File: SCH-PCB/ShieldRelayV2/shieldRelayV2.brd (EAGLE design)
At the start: 99.1 x 84.1 mm, 90 parts, among them IC1 LM2596SX-5.0_NOPB, IC2 LM1117MPX-33NOPB, IC3 FT231XS-R, K1 SLA-05VDC-SL-C, K2 SRD-05VDC-SL-C, K3 G3MB-202PL-DC5, K5 G3MB-202PL-DC5, K6 SRD-05VDC-SL-C, Q1 MMST2222A-7-F, Q2 MMST2222A-7-F, Q3 MMST2222A-7-F, Q4 MMST2222A-7-F, Q5 MMST2222A-7-F, Q6 MMBT3904-TP, Q7 MMBT3904-TP

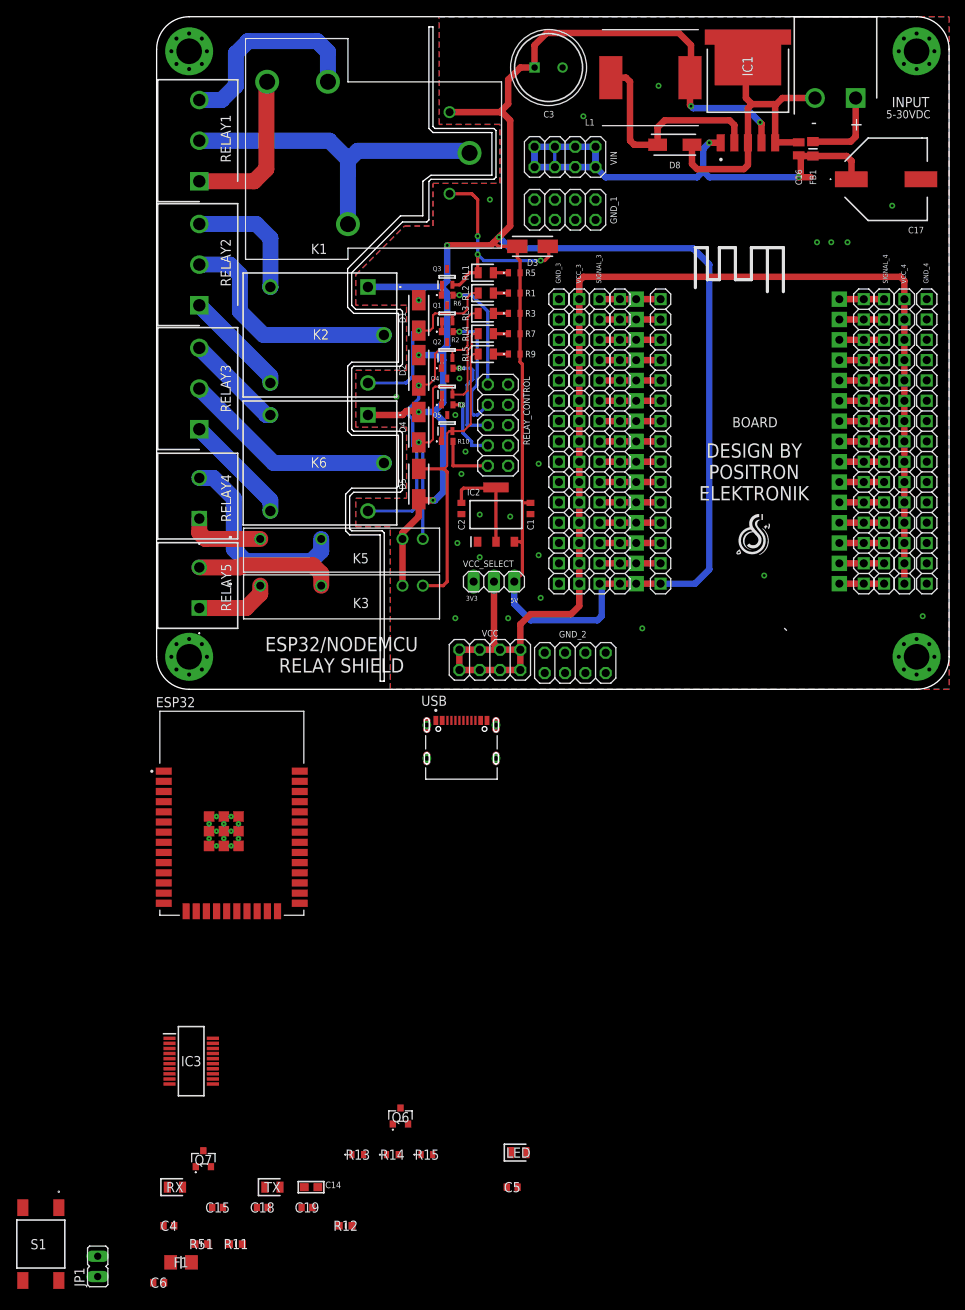
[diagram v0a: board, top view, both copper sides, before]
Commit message: FEAT: update sch, board, gerber adn bom for esp embedded to pcb
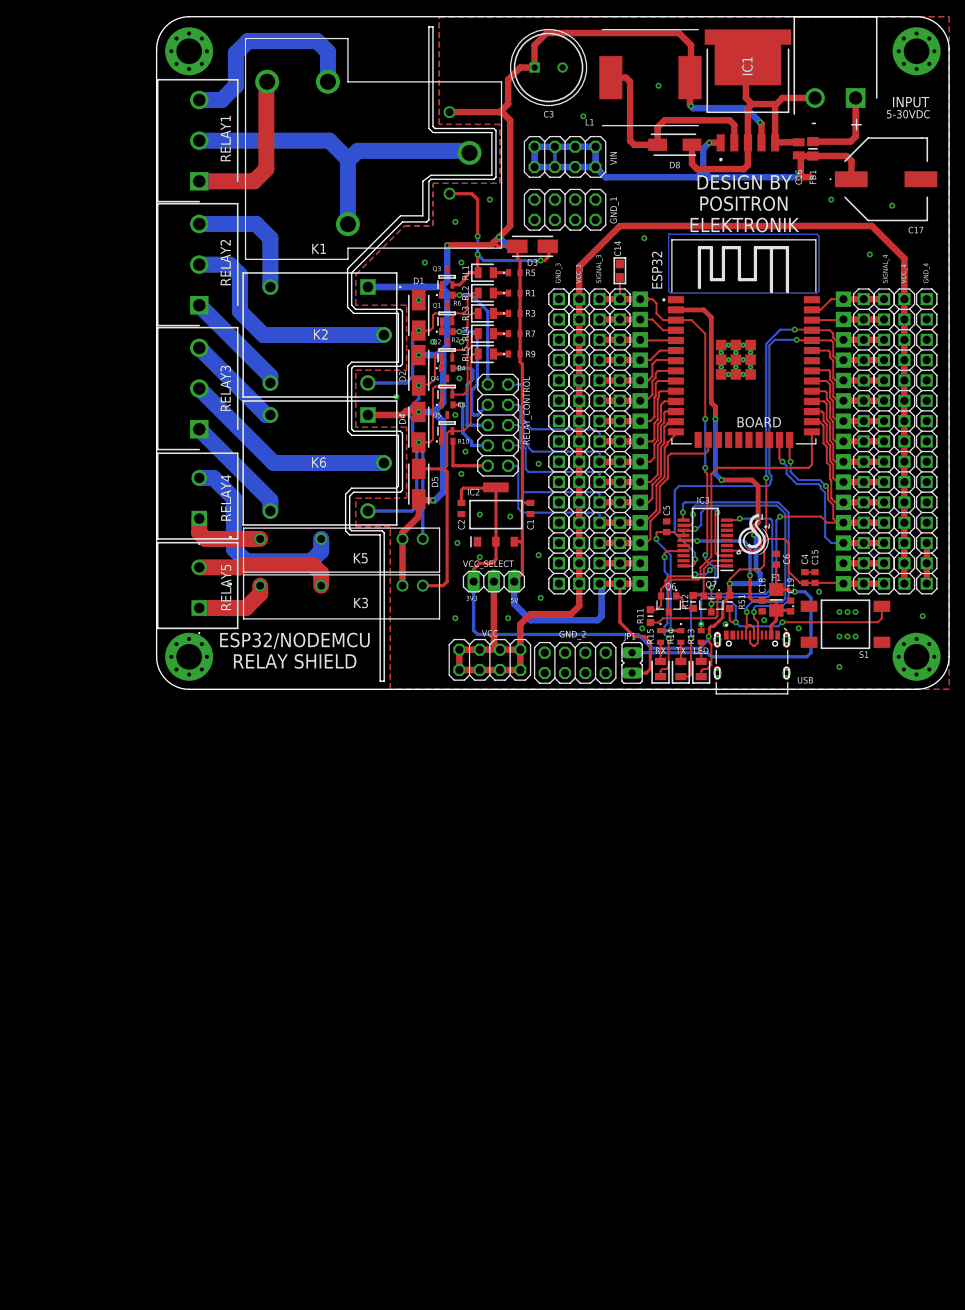
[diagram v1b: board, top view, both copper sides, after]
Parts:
- removed JP13: (no value), pinhead_mod:1X15
- moved S1 127.0 mm to (86.1, 24.1), turned to 90 degrees
- moved C14 120.9 mm to (57.9, 68.3), turned to 90 degrees
- moved C6 118.9 mm to (77.5, 32.3), turned to 90 degrees
- moved C4 113.5 mm to (81.0, 30.0), turned to 270 degrees
- moved F1 111.3 mm to (77.5, 27.2), turned to 90 degrees
- moved C15 108.5 mm to (82.3, 30.0), turned to 270 degrees
- moved R51 103.9 mm to (71.6, 26.9), turned to 270 degrees
- moved JP1 100.8 mm to (59.4, 19.3), turned to 180 degrees
- moved C18 97.8 mm to (75.7, 26.4), turned to 90 degrees
- moved C19 96.5 mm to (79.2, 26.4), turned to 90 degrees
- moved R11 94.0 mm to (61.7, 25.1), turned to 270 degrees
- moved Q7 94.0 mm to (69.3, 26.7), turned to 180 degrees
- moved IC3 91.2 mm to (68.6, 34.3), turned to 180 degrees
- moved R12 89.3 mm to (67.1, 26.9), turned to 270 degrees
- moved RX 88.8 mm to (63.0, 18.5), turned to 90 degrees
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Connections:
- removed net 1: BOARD.3V3, JP11.1, SIGNAL_4.1
- removed net 2: BOARD.GND@1, JP11.2, SIGNAL_4.2
- removed net 3.3V: C15.2, C4.2, ESP32.2, LED.1, R51.1
- removed net 3V3_FTDI: IC3.3
- removed net BUTTON1: ESP32.30
- removed net D23: ESP32.37
- removed net D25: ESP32.10
- removed net D26: ESP32.11
- removed net D27: ESP32.12
- removed net D32: ESP32.8
- removed net D33: ESP32.9
- removed net D34: ESP32.6
- removed net D35: ESP32.7
- removed net D5: ESP32.29
- removed net EN: C14.1, ESP32.3, Q7.3, R51.2, S1.2
- removed net LED: ESP32.31, R13.1
- removed net N$23: RELAY_CONTROL.10
- removed net N$24: RELAY_CONTROL.8
- removed net N$25: RELAY_CONTROL.6
- removed net N$26: RELAY_CONTROL.4
- removed net N$27: RELAY_CONTROL.2
- removed net RX_DWM: ESP32.28
- removed net SCL: ESP32.36
- removed net SDA: ESP32.33
- removed net SD_HOST_CLK: ESP32.13
- removed net SD_HOST_CMD: ESP32.23
- removed net SD_HOST_D0: ESP32.24
- removed net SD_HOST_D1: ESP32.26
- removed net SD_HOST_D2: ESP32.14
- removed net SD_HOST_D3: ESP32.16
- removed net TX_DWM: ESP32.27
- removed net U0RXD: ESP32.34, IC3.20
- removed net U0TXD: ESP32.35, IC3.4
- removed net VN: ESP32.5
- removed net VP: ESP32.4
- net +3V3: now also BOARD.3V3, C15.2, C4.2, ESP32.2, JP11.1, LED.1, R51.1, SIGNAL_4.1
- net +5V: no longer JP13.1
- net 10: now also ESP32.31
- net 11: now also ESP32.33
- net 12: now also ESP32.34, IC3.20
- net 13: now also ESP32.35, IC3.4
- net 14: now also ESP32.36
- net 15: now also ESP32.37
- net 18: now also ESP32.16; no longer JP13.3
- net 19: now also ESP32.14, RELAY_CONTROL.10; no longer JP13.4
- net 20: now also ESP32.13, RELAY_CONTROL.8; no longer JP13.5
- net 21: now also ESP32.12, RELAY_CONTROL.6; no longer JP13.6
- net 22: now also ESP32.11, RELAY_CONTROL.4; no longer JP13.7
- net 23: now also ESP32.10, RELAY_CONTROL.2; no longer JP13.8
- net 24: now also ESP32.9; no longer JP13.9
- net 25: now also ESP32.8; no longer JP13.10
- net 26: now also ESP32.7; no longer JP13.11
- net 27: now also ESP32.6; no longer JP13.12
- net 28: now also ESP32.5; no longer JP13.13
- net 29: now also ESP32.4; no longer JP13.14
- net 3: now also ESP32.23
- net 30: now also C14.1, ESP32.3, Q7.3, R51.2, S1.2; no longer JP13.15
- net 3V3_OUT: now also IC3.3
- net 4: now also ESP32.24, R13.1
- net 5: now also ESP32.26
- net 6: now also ESP32.27
- net 7: now also ESP32.28
- net 8: now also ESP32.29
- net 9: now also ESP32.30
- net GND: now also BOARD.GND@1, JP11.2, SIGNAL_4.2; no longer JP13.2
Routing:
- net +3V3: track 12.8 -> 145.8 mm, vias 0 -> 5
- net 30: track 7.62 -> 82.4 mm, vias 0 -> 7
- net +5V: track 302.4 -> 244.7 mm
- net 12: track 5.59 -> 58.2 mm, vias 0 -> 2
- net N$21: track 0.00 -> 51.9 mm
- net 4: track 5.59 -> 50.8 mm, vias 0 -> 4
- net 13: track 5.59 -> 46.4 mm, vias 0 -> 2
- net 0: track 0.00 -> 38.7 mm
- net D+: track 0.00 -> 38.3 mm, vias 0 -> 2
- net VBUS_: track 0.00 -> 37.5 mm, vias 0 -> 1
- net D-: track 0.00 -> 36.7 mm, vias 0 -> 2
- net CBUS2: track 0.00 -> 35.9 mm, vias 0 -> 2
- net 3V3_OUT: track 0.00 -> 33.0 mm, vias 0 -> 4
- net 19: track 7.62 -> 36.5 mm
- net 20: track 7.62 -> 36.1 mm
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
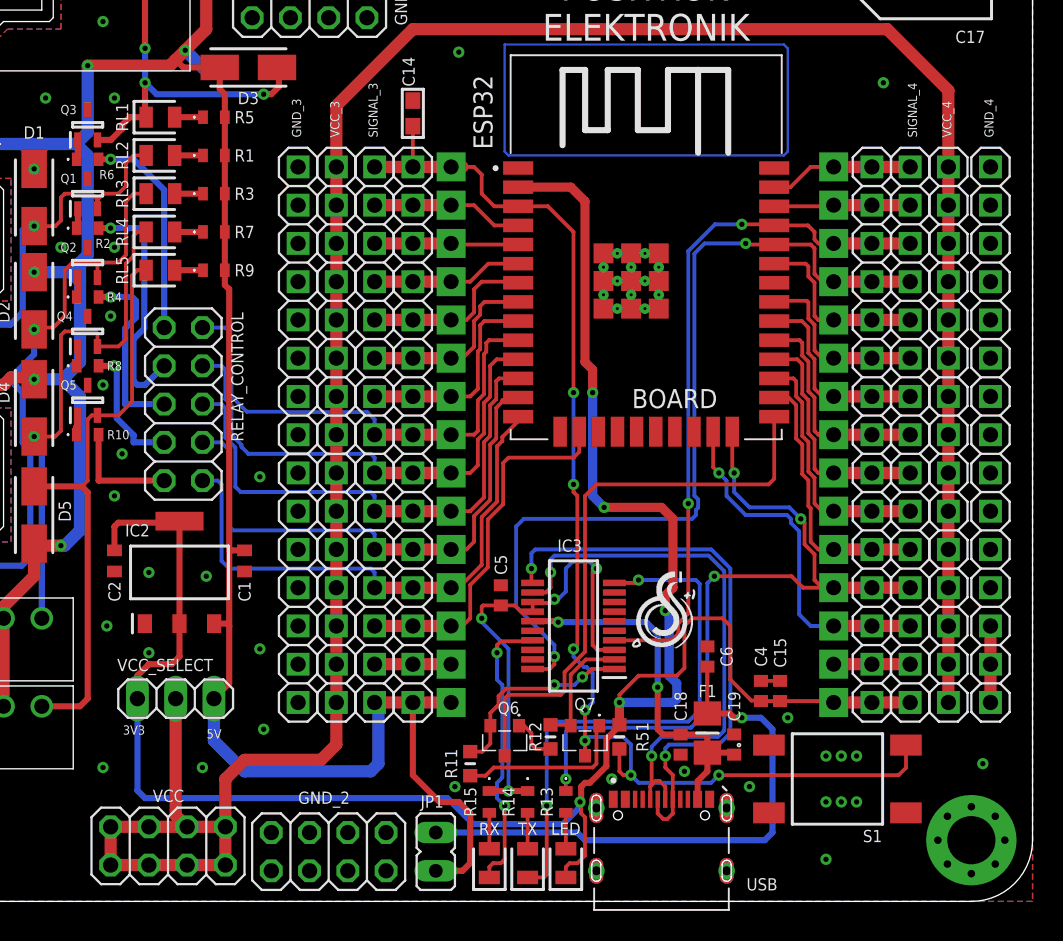
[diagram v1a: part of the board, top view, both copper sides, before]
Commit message: FIX: fix minor pcb
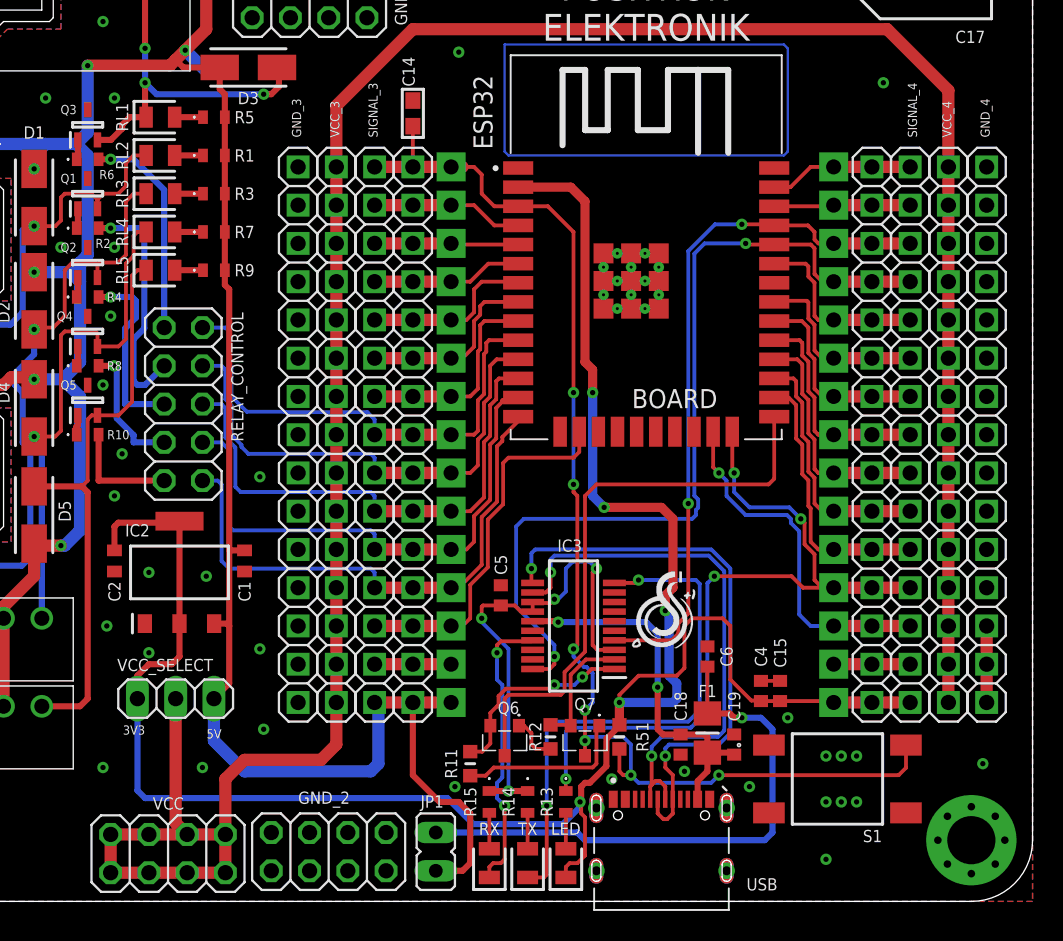
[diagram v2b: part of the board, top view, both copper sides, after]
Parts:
- moved VCC 0.51 mm to (41.7, 19.2)
- moved GND_4 0.25 mm to (96.0, 47.0)
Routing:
- net N$39: track 168.1 -> 169.1 mm
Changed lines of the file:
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@@
 <drawing>
 <settings>
-<setting alwaysvectorfont="yes"/>
+<setting alwaysvectorfont="no"/>
 <setting verticaltext="up"/>
 </settings>
@@
 <attribute name="VALUE" x="96.647" y="27.94" size="1.27" layer="27" rot="R90"/>
 </element>
-<element name="GND_4" library="pinhead_mod" package="1X15" package3d_urn="urn:adsk.eagle:package:22424/2" value="" x="96.266" y="46.99" smashed="yes" rot="R270">
-<attribute name="NAME" x="96.4692" y="66.7258" size="0.6096" layer="25" ratio="10" rot="R90"/>
-<attribute name="POPULARITY" value="4" x="96.266" y="46.99" size="1.778" layer="27" rot="R270" display="off"/>
-<attribute name="VALUE" x="93.091" y="66.04" size="1.27" layer="27" rot="R270"/>
+<element name="GND_4" library="pinhead_mod" package="1X15" package3d_urn="urn:adsk.eagle:package:22424/2" value="" x="96.012" y="46.99" smashed="yes" rot="R270">
+<attribute name="NAME" x="96.2152" y="66.7258" size="0.6096" layer="25" ratio="10" rot="R90"/>
+<attribute name="POPULARITY" value="4" x="96.012" y="46.99" size="1.778" layer="27" rot="R270" display="off"/>
+<attribute name="VALUE" x="92.837" y="66.04" size="1.27" layer="27" rot="R270"/>
 </element>
 <element name="GND_3" library="pinhead_mod" package="1X15" package3d_urn="urn:adsk.eagle:package:22424/2" value="" x="50.292" y="46.99" smashed="yes" rot="R270">
@@
 <attribute name="VALUE" x="45.974" y="32.639" size="1.27" layer="27" rot="R180"/>
 </element>
-<element name="VCC" library="pinhead" library_urn="urn:adsk.eagle:library:325" package="2X04" package3d_urn="urn:adsk.eagle:package:22461/2" value="" x="41.656" y="19.685" smashed="yes">
-<attribute name="NAME" x="40.64" y="22.606" size="0.8128" layer="25" ratio="10"/>
-<attribute name="POPULARITY" value="47" x="41.656" y="19.685" size="1.778" layer="27" display="off"/>
-<attribute name="VALUE" x="36.576" y="15.24" size="1.27" layer="27"/>
+<element name="VCC" library="pinhead" library_urn="urn:adsk.eagle:library:325" package="2X04" package3d_urn="urn:adsk.eagle:package:22461/2" value="" x="41.656" y="19.177" smashed="yes">
+<attribute name="NAME" x="40.64" y="22.098" size="0.8128" layer="25" ratio="10"/>
+<attribute name="POPULARITY" value="47" x="41.656" y="19.177" size="1.778" layer="27" display="off"/>
+<attribute name="VALUE" x="36.576" y="14.732" size="1.27" layer="27"/>
 </element>
 <element name="GND_2" library="pinhead" library_urn="urn:adsk.eagle:library:325" package="2X04" package3d_urn="urn:adsk.eagle:package:22461/2" value="" x="52.324" y="19.304" smashed="yes">
@@
 <wire x1="85.852" y1="31.75" x2="88.392" y2="31.75" width="0.8128" layer="1"/>
 <wire x1="90.932" y1="31.75" x2="88.392" y2="31.75" width="0.8128" layer="1"/>
-<wire x1="96.266" y1="31.75" x2="96.266" y2="34.29" width="0.8128" layer="1"/>
-<wire x1="96.266" y1="29.21" x2="96.266" y2="31.75" width="0.8128" layer="1"/>
+<wire x1="96.012" y1="31.75" x2="96.012" y2="34.29" width="0.8128" layer="1"/>
+<wire x1="96.012" y1="29.21" x2="96.012" y2="31.75" width="0.8128" layer="1"/>
 <via x="85.344" y="22.606" extent="1-16" drill="0.35"/>
 <via x="85.344" y="25.654" extent="1-16" drill="0.35"/>
@@
 <contactref element="VCC" pad="3"/>
 <contactref element="VCC" pad="1"/>
-<wire x1="42.164" y1="29.464" x2="42.164" y2="21.717" width="0.8128" layer="1"/>
-<wire x1="42.164" y1="21.717" x2="42.926" y2="20.955" width="0.8128" layer="1"/>
-<wire x1="40.386" y1="20.955" x2="42.926" y2="20.955" width="0.8128" layer="1"/>
-<wire x1="40.386" y1="20.955" x2="37.846" y2="20.955" width="0.8128" layer="1"/>
-<wire x1="37.846" y1="20.955" x2="37.846" y2="18.415" width="0.8128" layer="1"/>
-<wire x1="37.846" y1="18.415" x2="40.386" y2="18.415" width="0.8128" layer="1"/>
-<wire x1="40.386" y1="18.415" x2="42.926" y2="18.415" width="0.8128" layer="1"/>
-<wire x1="42.926" y1="18.415" x2="45.466" y2="18.415" width="0.8128" layer="1"/>
-<wire x1="45.466" y1="18.415" x2="45.466" y2="20.955" width="0.8128" layer="1"/>
-<wire x1="45.466" y1="20.955" x2="42.926" y2="20.955" width="0.8128" layer="1"/>
+<wire x1="42.164" y1="29.464" x2="42.164" y2="21.209" width="0.8128" layer="1"/>
+<wire x1="42.164" y1="21.209" x2="42.926" y2="20.447" width="0.8128" layer="1"/>
+<wire x1="40.386" y1="20.447" x2="42.926" y2="20.447" width="0.8128" layer="1"/>
+<wire x1="40.386" y1="20.447" x2="37.846" y2="20.447" width="0.8128" layer="1"/>
+<wire x1="37.846" y1="20.447" x2="37.846" y2="17.907" width="0.8128" layer="1"/>
+<wire x1="37.846" y1="17.907" x2="40.386" y2="17.907" width="0.8128" layer="1"/>
+<wire x1="40.386" y1="17.907" x2="42.926" y2="17.907" width="0.8128" layer="1"/>
+<wire x1="42.926" y1="17.907" x2="45.466" y2="17.907" width="0.8128" layer="1"/>
+<wire x1="45.466" y1="17.907" x2="45.466" y2="20.447" width="0.8128" layer="1"/>
+<wire x1="45.466" y1="20.447" x2="42.926" y2="20.447" width="0.8128" layer="1"/>
 <wire x1="51.816" y1="25.4" x2="52.832" y2="26.416" width="0.8128" layer="1"/>
 <wire x1="52.832" y1="26.416" x2="52.832" y2="29.21" width="0.8128" layer="1"/>
@@
 <wire x1="93.472" y1="34.29" x2="93.472" y2="31.75" width="0.8128" layer="1"/>
 <wire x1="93.472" y1="29.21" x2="93.472" y2="31.75" width="0.8128" layer="1"/>
-<wire x1="45.466" y1="20.955" x2="45.466" y2="24.13" width="0.8128" layer="1"/>
+<wire x1="45.466" y1="20.447" x2="45.466" y2="24.13" width="0.8128" layer="1"/>
 <wire x1="45.466" y1="24.13" x2="46.736" y2="25.4" width="0.8128" layer="1"/>
 <wire x1="46.736" y1="25.4" x2="51.816" y2="25.4" width="0.8128" layer="1"/>

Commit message: FIX: fix gnd pin on ic 1117 that no connected
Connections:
- net GND: now also IC2.1
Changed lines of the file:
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@@
 </layers>
 <board>
-<fusionsync huburn="a.YnVzaW5lc3M6Z21haWwyMzM3NTk" projecturn="a.YnVzaW5lc3M6Z21haWwyMzM3NTkjRDIwMTkwNzEwMjAyOTg4NzI2" f3durn="urn:adsk.wipprod:dm.lineage:9T0BP-n2RnCNxMkO3_9ujQ" pcbguid="" lastpulledtime="" lastsyncedchangeguid="" latestrevisionid="43e5cbbb-d091-4418-b876-1ea316f0a193" lastsyncedrevisionid="43e5cbbb-d091-4418-b876-1ea316f0a193" lastboardhashguid="19c69a16-bb44-e2b6-368f-cff3622da438" lastpushedtime="2024-06-15T15:23:29Z" linktopcb3d="true"/>
+<fusionsync huburn="a.YnVzaW5lc3M6Z21haWwyMzM3NTk" projecturn="a.YnVzaW5lc3M6Z21haWwyMzM3NTkjRDIwMTkwNzEwMjAyOTg4NzI2" f3durn="urn:adsk.wipprod:dm.lineage:9T0BP-n2RnCNxMkO3_9ujQ" pcbguid="" lastpulledtime="" lastsyncedchangeguid="" latestrevisionid="43e5cbbb-d091-4418-b876-1ea316f0a193" lastsyncedrevisionid="43e5cbbb-d091-4418-b876-1ea316f0a193" lastboardhashguid="19c69a16-bb44-e2b6-368f-cff3622da438" lastpushedtime="2024-06-15T15:23:29Z" linktopcb3d="false"/>
 <plain>
 <wire x1="78.74" y1="23.368" x2="78.486" y2="23.622" width="0.1524" layer="21"/>
@@
 <via x="38.1" y="59.436" extent="1-16" drill="0.35"/>
 <via x="34.544" y="59.436" extent="1-16" drill="0.35"/>
+<contactref element="IC2" pad="1"/>
 </signal>
 <signal name="N$2">
